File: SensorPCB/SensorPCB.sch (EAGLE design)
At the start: 33 parts

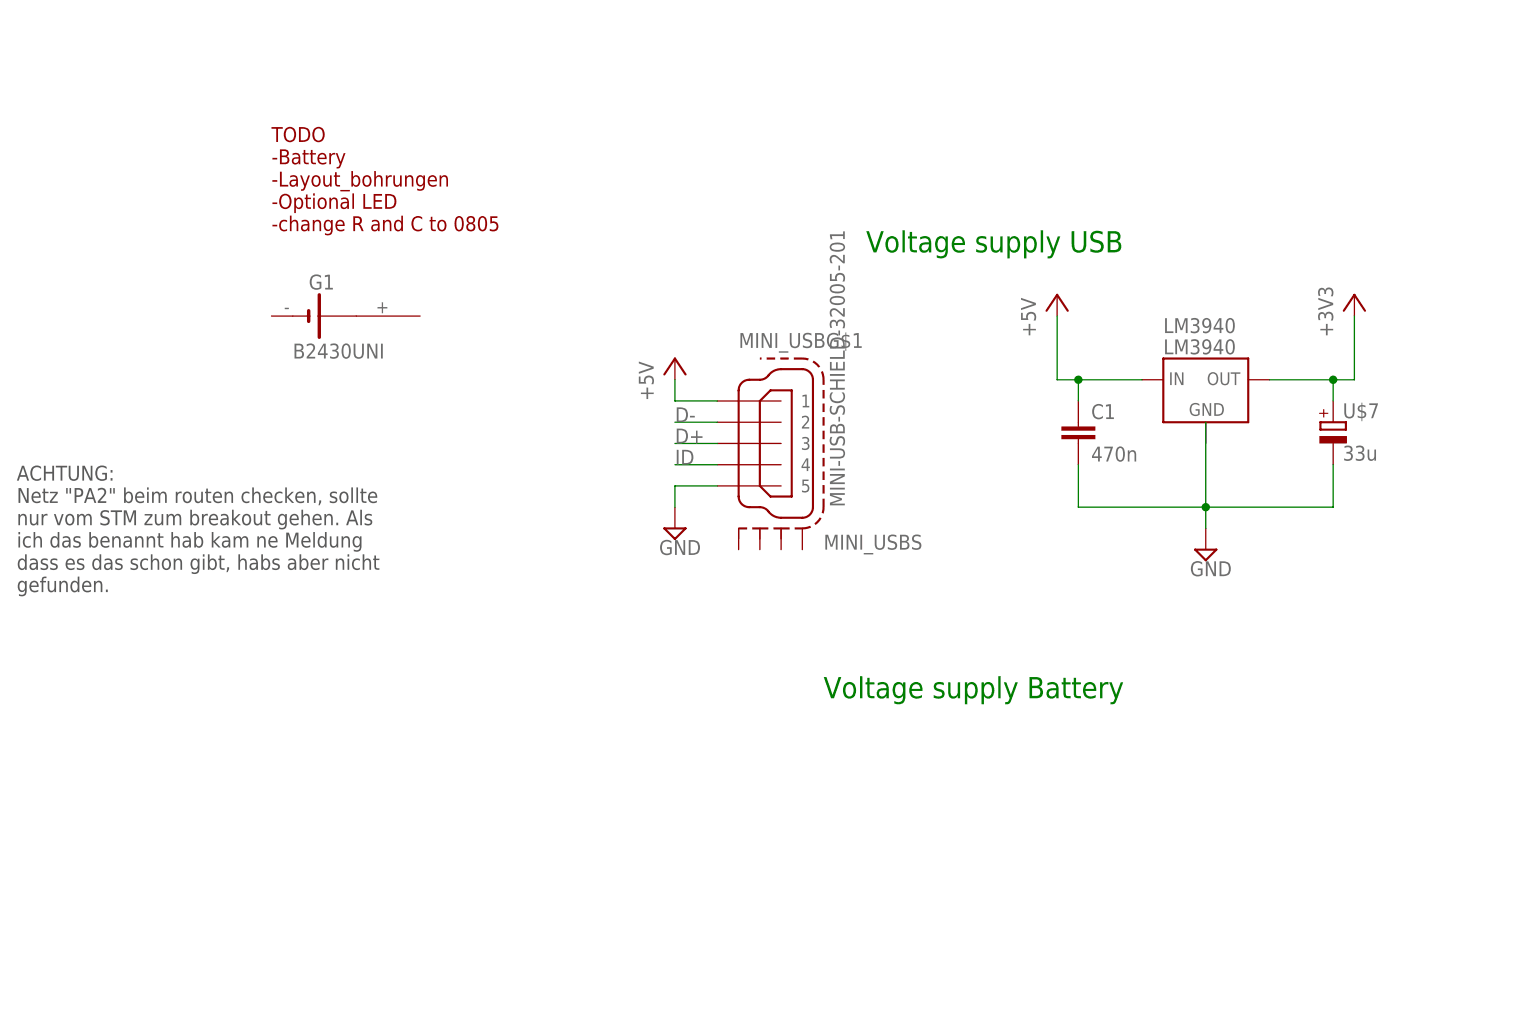
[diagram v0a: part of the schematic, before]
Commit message: some updates + add second gnd-pad for voltage regulator
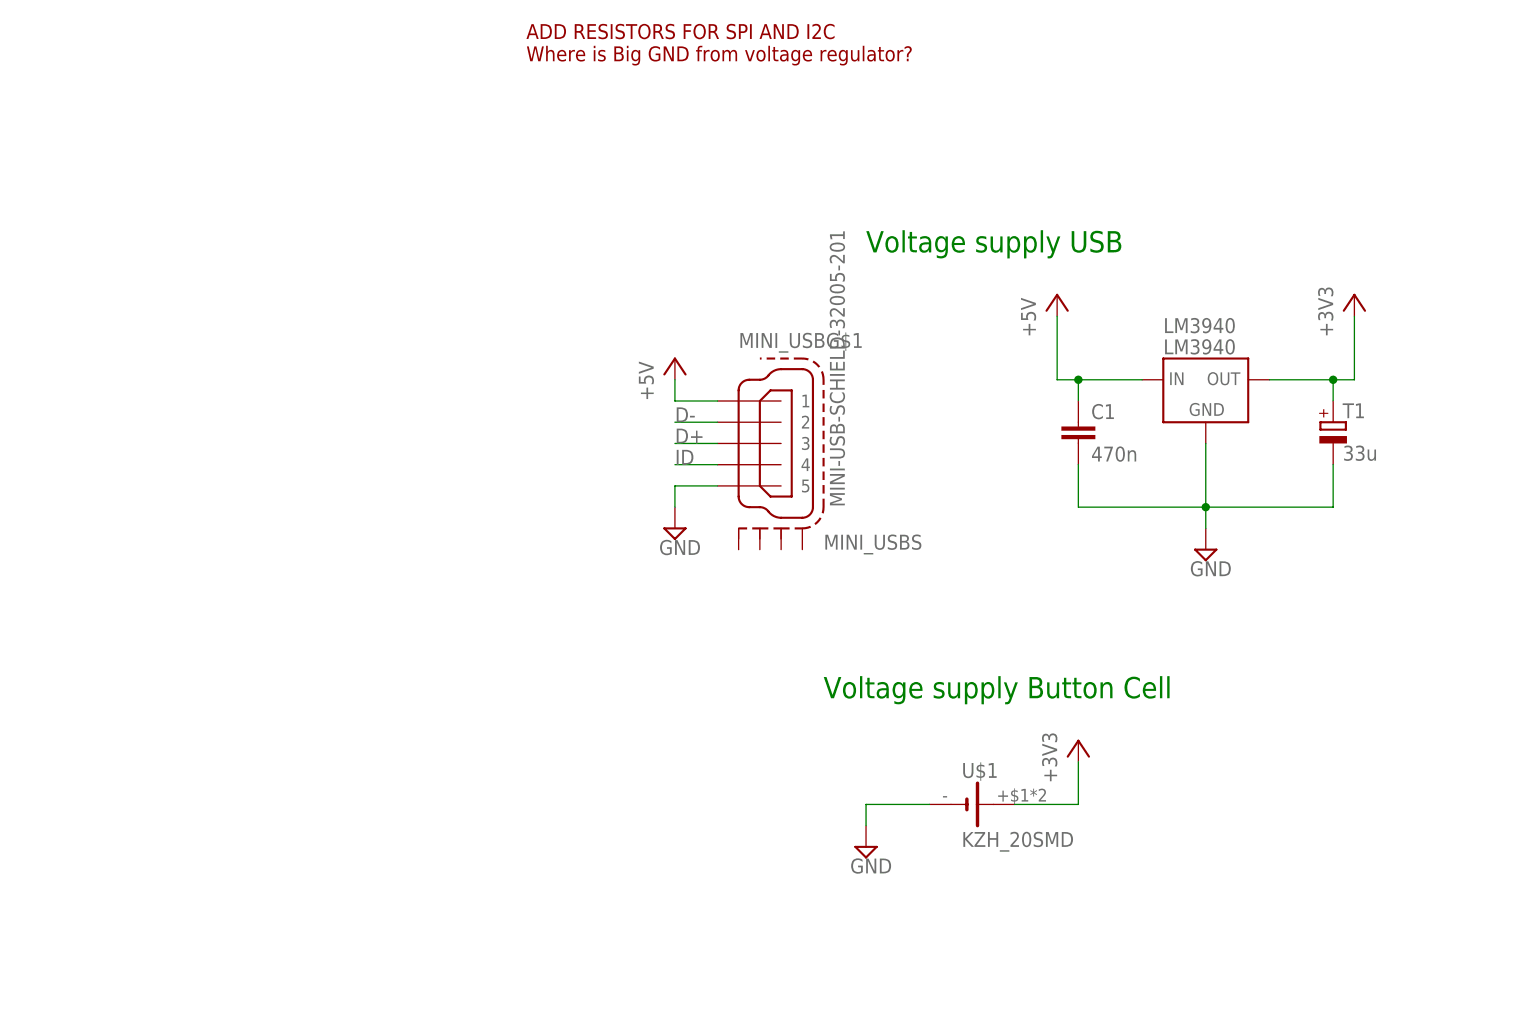
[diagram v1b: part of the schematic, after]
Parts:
- removed G1: B2430UNI, battery:B2430UNI
- added U$1: KZH_20SMD, KZH_20SMD:KZH_20SMD
- renumbered U$7 to T1
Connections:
- net +3V3: now also U$1.+
- net GND: now also LM3940.GND, U$1.-
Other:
- note added: "ADD RESISTORS FOR SPI AND I2C Where is Big GND from voltage regulator?"
- note added: "Voltage supply Button Cell"
- note removed: "ACHTUNG: Netz "PA2" beim routen checken, sollte nur vom STM zum breakout gehen. Als ich das benannt hab kam ne Meldung dass es das schon gibt, habs aber nicht gefunden."
- note removed: "TODO -Battery -Layout_bohrungen -Optional LED -change R and C to 0805"
- note removed: "Voltage supply Battery"

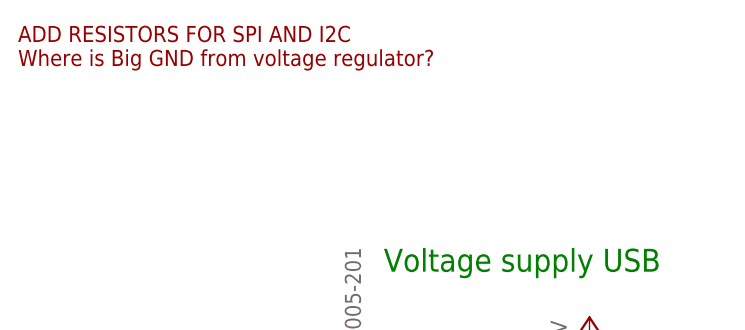
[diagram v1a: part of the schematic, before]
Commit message: change STM32 footprint (tstop tcream)
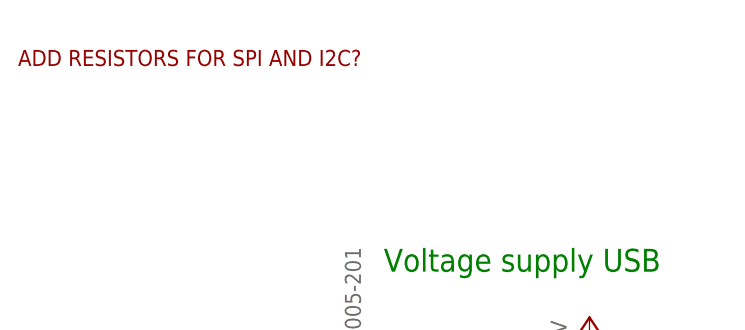
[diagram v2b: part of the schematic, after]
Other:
- note added: "ADD RESISTORS FOR SPI AND I2C?"
- note removed: "ADD RESISTORS FOR SPI AND I2C Where is Big GND from voltage regulator?"
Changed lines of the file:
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@@
 <text x="302.26" y="50.8" size="1.778" layer="91" rot="R90">I2C address
 0011000</text>
-<text x="0" y="266.7" size="1.778" layer="94">ADD RESISTORS FOR SPI AND I2C
-Where is Big GND from voltage regulator?</text>
+<text x="0" y="266.7" size="1.778" layer="94">ADD RESISTORS FOR SPI AND I2C?
+</text>
 </plain>
 <instances>
